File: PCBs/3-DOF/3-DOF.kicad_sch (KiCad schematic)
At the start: 19 parts, among them J1 Conn_02x07_Odd_Even, J10 Conn_01x06, J11 Conn_01x04, J12 Conn_01x04, J2 Conn_02x08_Odd_Even, J3 Conn_02x08_Odd_Even, J4 Conn_01x02, J5 Conn_01x02, J6 Conn_01x06, J7 Conn_01x06, J8 Conn_01x06, J9 Conn_01x04, U1 MAX485E, U2 L298N, U3 L298N

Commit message: updated with laser + servo + 485MAX (corrected
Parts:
- added C5: 10u, Capacitor_SMD:C_0402_1005Metric_Pad0.74x0.62mm_HandSolder, symbol Device:C
- added J13: Conn_01x03, Connector_JST:JST_XH_S3B-XH-A_1x03_P2.50mm_Horizontal, symbol Connector_Generic:Conn_01x03
- added J14, J15, J16, J17, J18: Conn_01x04, Connector_JST:JST_XH_S4B-XH-A_1x04_P2.50mm_Horizontal, symbol Connector_Generic:Conn_01x04
- added Q1: 2N7000, Package_TO_SOT_THT:TO-92_Inline, symbol Transistor_FET:2N7000
- added R1: 1k, Resistor_SMD:R_0402_1005Metric_Pad0.72x0.64mm_HandSolder, symbol Device:R_US
- added R2: 100, Resistor_SMD:R_0402_1005Metric_Pad0.72x0.64mm_HandSolder, symbol Device:R_US
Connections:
- net +5V: now also C5.2, J13.1 (Pin_1), J14.1 (Pin_1), J15.1 (Pin_1), J16.1 (Pin_1), J17.1 (Pin_1), J18.1 (Pin_1)
- net 16: now also J14.3 (Pin_3)
- net 17: now also J15.3 (Pin_3)
- net 20: now also J16.3 (Pin_3)
- net 56: now also R2.2
- net 59: now also J17.3 (Pin_3)
- net 62: now also J18.3 (Pin_3)
- net GND: now also C5.1, J13.2 (Pin_2), J14.2 (Pin_2), J15.2 (Pin_2), J16.2 (Pin_2), J17.2 (Pin_2), J18.2 (Pin_2), Q1.1 (S)
- net at J11.3 (Pin_3), J12.3 (Pin_3), J9.3 (Pin_3)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: now also R1.1
- net at J11.2 (Pin_2), J12.2 (Pin_2), J9.2 (Pin_2)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: now also R1.2
- new net: Q1.2 (G), R2.1
- new net: J13.3 (Pin_3), Q1.3 (D)
- no-connect marks 21 -> 15

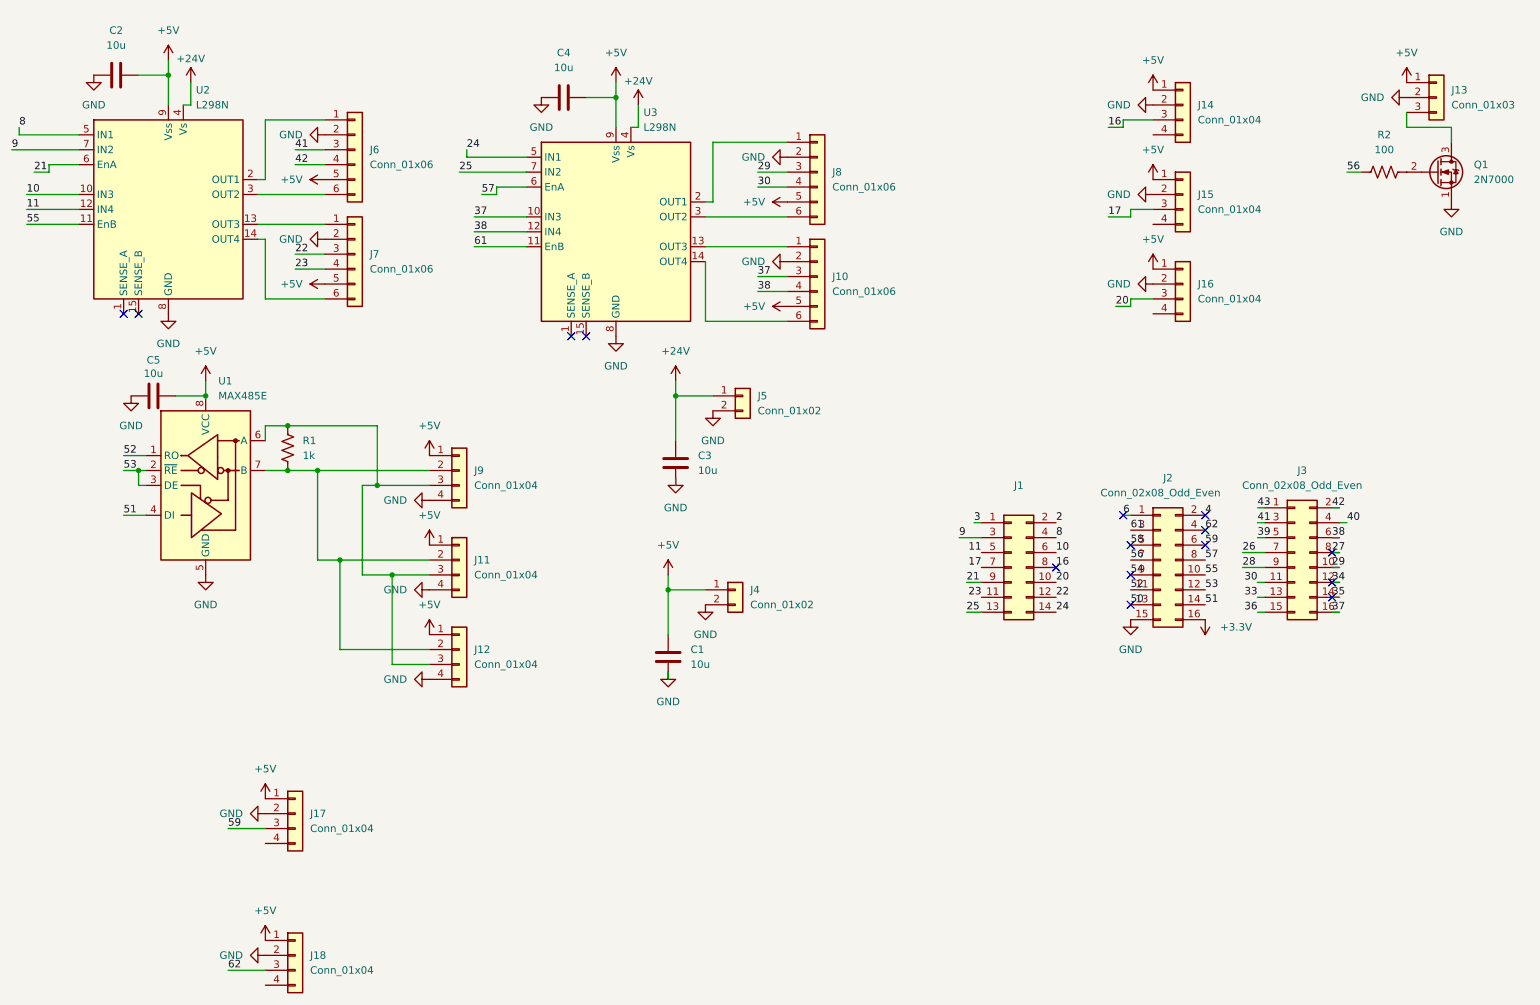
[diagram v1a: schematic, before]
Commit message: fix RS485 + servo, add 10u cap's
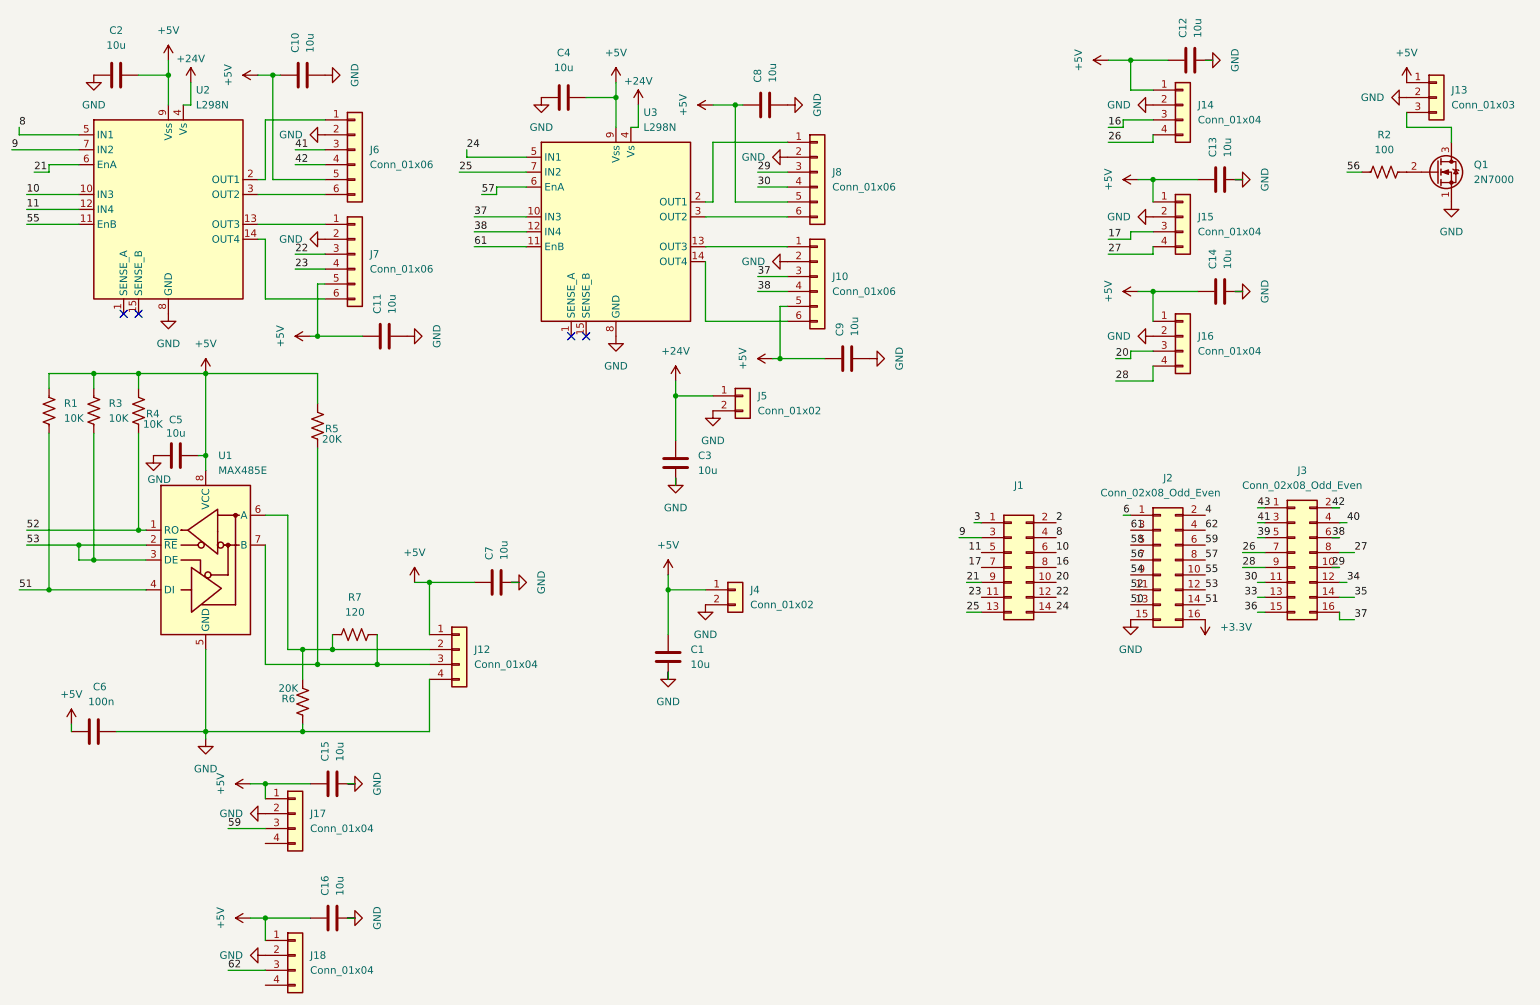
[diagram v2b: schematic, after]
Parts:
- removed J11, J9: Conn_01x04, Connector_JST:JST_XH_S4B-XH-A_1x04_P2.50mm_Horizontal, symbol Connector_Generic:Conn_01x04
- added C10, C11, C12, C13, C14, C15, C16, C7, C8, C9: 10u, Capacitor_SMD:C_0402_1005Metric_Pad0.74x0.62mm_HandSolder, symbol Device:C
- added C6: 100n, Capacitor_SMD:C_0402_1005Metric_Pad0.74x0.62mm_HandSolder, symbol Device:C
- added R3, R4: 10K, Resistor_SMD:R_0402_1005Metric_Pad0.72x0.64mm_HandSolder, symbol Device:R_US
- added R5, R6: 20K, Resistor_SMD:R_0402_1005Metric_Pad0.72x0.64mm_HandSolder, symbol Device:R_US
- added R7: 120, Resistor_SMD:R_0402_1005Metric_Pad0.72x0.64mm_HandSolder, symbol Device:R_US
- R1: value 1k -> 10K
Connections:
- net +5V: now also R1.1, C10.1, C11.1, C12.1, C13.1, C14.1, C15.1, C16.1, C6.2, C7.1, C8.1, C9.1, R3.1, R4.1, R5.1
- net 26: now also J14.4 (Pin_4)
- net 27: now also J15.4 (Pin_4)
- net 28: now also J16.4 (Pin_4)
- net 51: now also R1.2
- net 52: now also R4.2
- net 53: now also R3.2
- net GND: now also C10.2, C11.2, C12.2, C13.2, C14.2, C15.2, C16.2, C6.1, C7.2, C8.2, C9.2, R6.1
- new net: J12.3 (Pin_3), R5.2, R7.2, U1.7 (B)
- new net: J12.2 (Pin_2), R6.2, R7.1, U1.6 (A)
- no-connect marks 15 -> 4
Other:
- moved on the sheet: C5, J15, J16, U1
